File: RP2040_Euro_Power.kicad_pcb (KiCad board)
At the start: 2 copper layers, 110 x 110 mm, 150 parts, among them J1 Conn_01x40, J2 Conn_01x40, J3 Power, J4 USB C/USB 2.0, J5 Conn_01x03_Pin, SW1 SW_BOOT, SW2 SW_RESET, U1 78L05_SOT89, U2 W25Q128JVS, U3 TL431D, U4 AMS1117-3.3, U5 RP2040, U6 MCP6002, Y1 Crystal_12MHz_4Pin

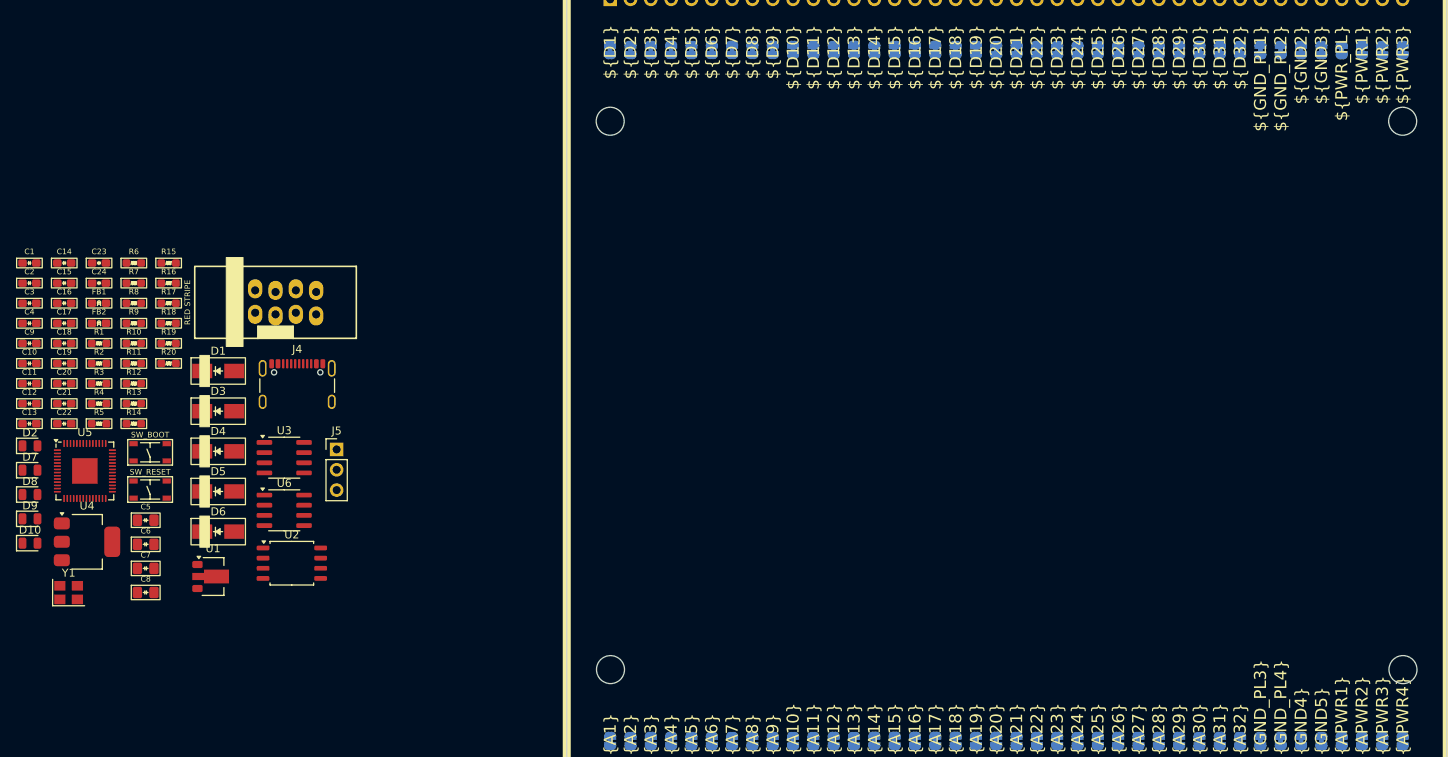
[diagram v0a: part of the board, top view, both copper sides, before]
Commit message: half of the parts placed on board
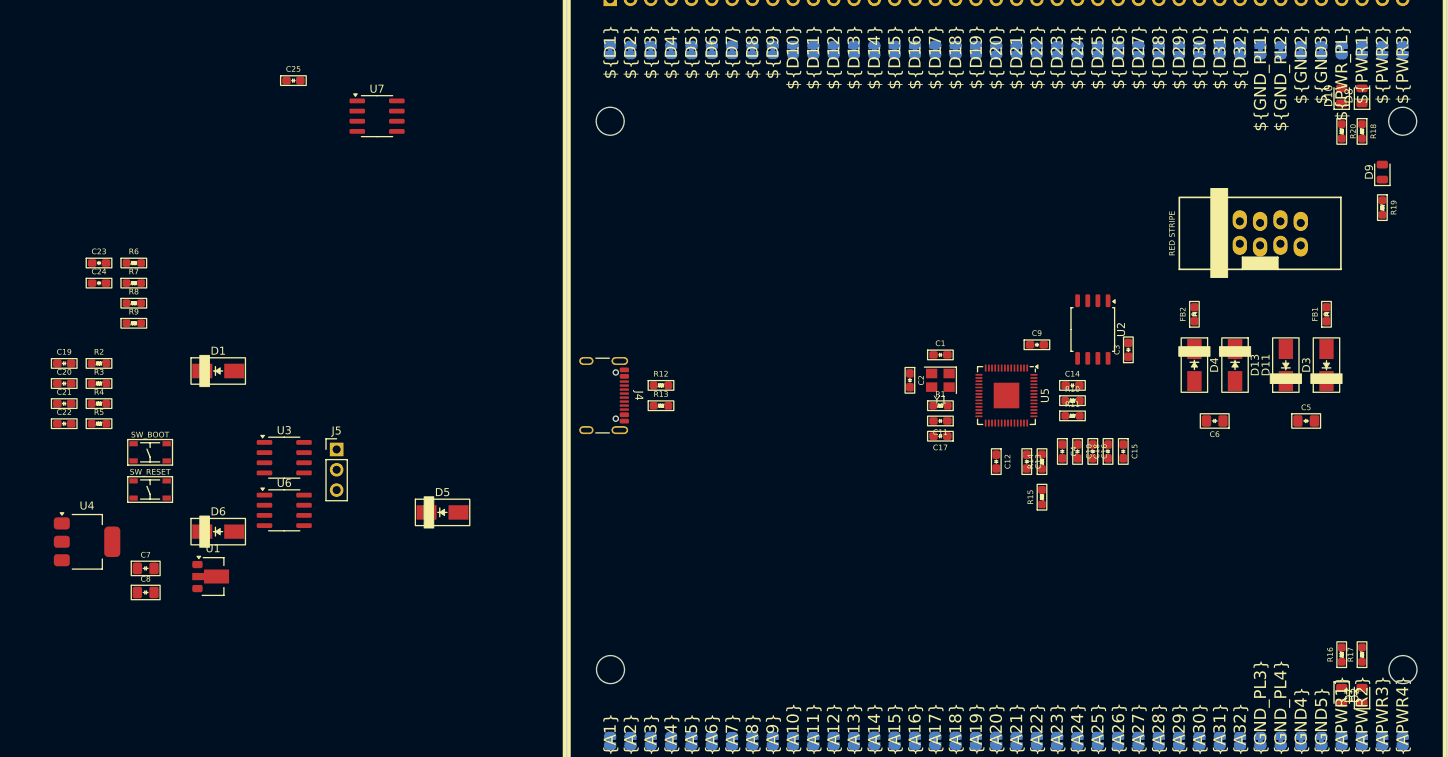
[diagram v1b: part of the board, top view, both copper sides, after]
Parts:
- added C25: 100n, winterbloom:C_0603_HandSolder, F.Cu at (39.8, 53.8)
- added D11: D_Schottky, winterbloom:D_SMA, F.Cu at (163.9, 89.4)
- added D13: D_Schottky, winterbloom:D_SMA, F.Cu at (157.5, 89.4)
- added U7: TL072, Package_SO:SOIC-8_3.9x4.9mm_P1.27mm, F.Cu at (50.3, 58.2)
- JP127, JP128, JP129, JP130: value ~ -> SolderJumper_2_Open; footprint Jumper:SolderJumper-2_P1.3mm_Bridged_RoundedPad1.0x1.5mm -> Jumper:SolderJumper-2_P1.3mm_Open_RoundedPad1.0x1.5mm
- R8: value 33k -> 47k
- moved D9 174.5 mm to (175.9, 65.2), turned to 90 degrees
- moved D8 173.8 mm to (173.4, 55.7), turned to 90 degrees
- moved D10 173.2 mm to (170.9, 55.7), turned to 90 degrees
- moved D7 168.9 mm to (173.4, 130.6), turned to 90 degrees
- moved D2 166.9 mm to (170.9, 130.6), turned to -90 degrees
- moved R17 155.5 mm to (173.4, 125.6), turned to 90 degrees
- moved R16 153.8 mm to (170.9, 125.6), turned to 90 degrees
- moved FB1 153.4 mm to (169.0, 83.0), turned to 90 degrees
- moved R19 152.7 mm to (175.9, 69.7), turned to -90 degrees
- moved R18 151.1 mm to (173.4, 60.2), turned to -90 degrees
- moved R20 149.5 mm to (170.9, 60.2), turned to -90 degrees
- moved C5 145.6 mm to (166.4, 96.3)
- moved D3 138.6 mm to (169.0, 89.4), turned to 90 degrees
- moved C3 137.5 mm to (144.2, 87.5), turned to 90 degrees
- moved FB2 136.9 mm to (152.5, 83.0), turned to 90 degrees
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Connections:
- C1 pad 1: GND -> GND_PLANE
- C10 pad 2: GND -> GND_PLANE
- C11 pad 2: GND -> GND_PLANE
- C12 pad 2: GND -> GND_PLANE
- C13 pad 2: GND -> GND_PLANE
- C14 pad 2: GND -> GND_PLANE
- C15 pad 2: GND -> GND_PLANE
- C16 pad 2: GND -> GND_PLANE
- C17 pad 2: GND -> GND_PLANE
- C18 pad 1: GND -> GND_PLANE
- C19 pad 1: PWR1 -> APWR1
- C19 pad 2: GND -> GND_PLANE
- C2 pad 1: GND -> GND_PLANE
- C20 pad 2: GND -> GND_PLANE
- C21 pad 2: GND -> GND_PLANE
- C22 pad 1: Net-(U6A--) -> Net-(U7A--)
- C22 pad 2: 3.3VREF -> 3VREF
- C23 pad 2: GND -> GND_PLANE
- C24 pad 2: GND -> GND_PLANE
- C3 pad 2: GND -> GND_PLANE
- C4 pad 2: GND -> GND_PLANE
- C5 pad 2: GND -> GND_PLANE
- C6 pad 2: GND -> GND_PLANE
- C7 pad 2: GND -> GND_PLANE
- C8 pad 2: GND -> GND_PLANE
- C9 pad 2: GND -> GND_PLANE
- D10 pad 1: GND -> Net-(D10-K)
- D10 pad 2: Net-(D10-A) -> IOVDD
- D2 pad 1: GND -> Net-(D2-K)
- D2 pad 2: Net-(D2-A) -> APWR1
- D7 pad 1: Net-(D7-K) -> APWR2
- D7 pad 2: GND -> Net-(D7-A)
- D8 pad 1: GND -> Net-(D8-K)
- D8 pad 2: Net-(D8-A) -> PWR1
- D9 pad 1: GND -> Net-(D9-K)
- D9 pad 2: Net-(D9-A) -> PWR2
- J3 pad 3: GND -> GND_PLANE
- J3 pad 4: GND -> GND_PLANE
- J3 pad 5: GND -> GND_PLANE
- J3 pad 6: GND -> GND_PLANE
- J3 pad 7: GND -> GND_PLANE
- J3 pad 8: GND -> GND_PLANE
- J4 pad A1: GND -> GND_PLANE
- J4 pad A12: GND -> GND_PLANE
- J4 pad B1: GND -> GND_PLANE
- J4 pad B12: GND -> GND_PLANE
- J4 pad S1: GND -> GND_PLANE
- J5 pad 1: SWCLK -> D27
- J5 pad 2: GND -> GND_PLANE
- J5 pad 3: SWD -> D28
- JP127 pad 1: Net-(J1-Pin_27) -> D27
- JP127 pad 2: D27 -> Net-(J1-Pin_27)
- JP128 pad 1: Net-(J1-Pin_28) -> D28
- JP128 pad 2: D28 -> Net-(J1-Pin_28)
- JP129 pad 1: Net-(J1-Pin_29) -> D29
- JP129 pad 2: D29 -> Net-(J1-Pin_29)
- JP130 pad 1: Net-(J1-Pin_30) -> BOOT
- JP130 pad 2: D30 -> Net-(J1-Pin_30)
- JP140 pad 2: 3.3VREF -> 3VREF
- R12 pad 2: GND -> GND_PLANE
- R13 pad 2: GND -> GND_PLANE
- R14 pad 1: 3.3VREF -> 3VREF
- R15 pad 2: 3.3VREF -> 3VREF
- R16 pad 1: APWR1 -> Net-(D2-K)
- R16 pad 2: Net-(D2-A) -> GND_PLANE
- R17 pad 1: APWR2 -> Net-(D7-A)
- R17 pad 2: Net-(D7-K) -> GND_PLANE
- R18 pad 1: PWR1 -> Net-(D8-K)
- R18 pad 2: Net-(D8-A) -> GND_PLANE
- R19 pad 1: PWR2 -> Net-(D9-K)
- R19 pad 2: Net-(D9-A) -> GND_PLANE
- R2 pad 1: Net-(SW1-A) -> BOOT
- R20 pad 1: IOVDD -> Net-(D10-K)
- R20 pad 2: Net-(D10-A) -> GND_PLANE
- R3 pad 2: Net-(SW1-A) -> BOOT
- R5 pad 1: Net-(SW1-A) -> BOOT
- R6 pad 1: RUN -> D29
- R7 pad 1: Net-(U6A--) -> Net-(U7A--)
- R7 pad 2: 3.3VREF -> 3VREF
- R8 pad 1: GND -> GND_PLANE
- R8 pad 2: Net-(U6A--) -> Net-(U7A--)
- SW1 pad 1: Net-(SW1-A) -> BOOT
- SW1 pad 2: GND -> GND_PLANE
- SW2 pad 1: RUN -> D29
- SW2 pad 2: GND -> GND_PLANE
- U1 pad 2: GND -> GND_PLANE
- U2 pad 4: GND -> GND_PLANE
- U3 pad 2: GND -> GND_PLANE
- U3 pad 3: GND -> GND_PLANE
- U3 pad 6: GND -> GND_PLANE
- U3 pad 7: GND -> GND_PLANE
- U4 pad 1: GND -> GND_PLANE
- U5 pad 19: GND -> GND_PLANE
- U5 pad 24: SWCLK -> D27
- U5 pad 25: SWD -> D28
- U5 pad 26: RUN -> D29
- U5 pad 57: GND -> GND_PLANE
- Y1 pad 2: GND -> GND_PLANE
- Y1 pad 4: GND -> GND_PLANE

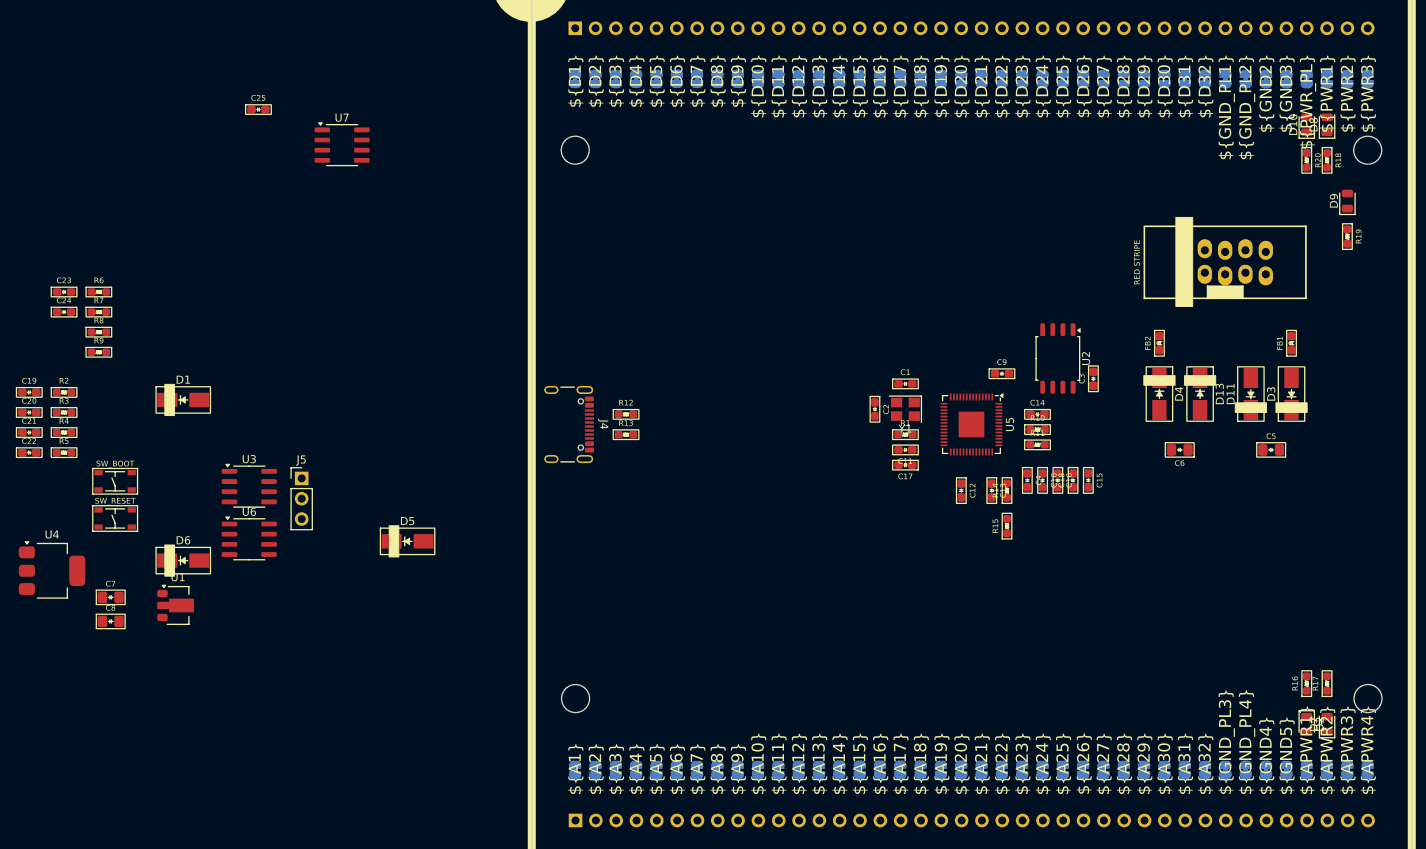
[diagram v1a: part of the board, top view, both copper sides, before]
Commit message: all parts placed on board
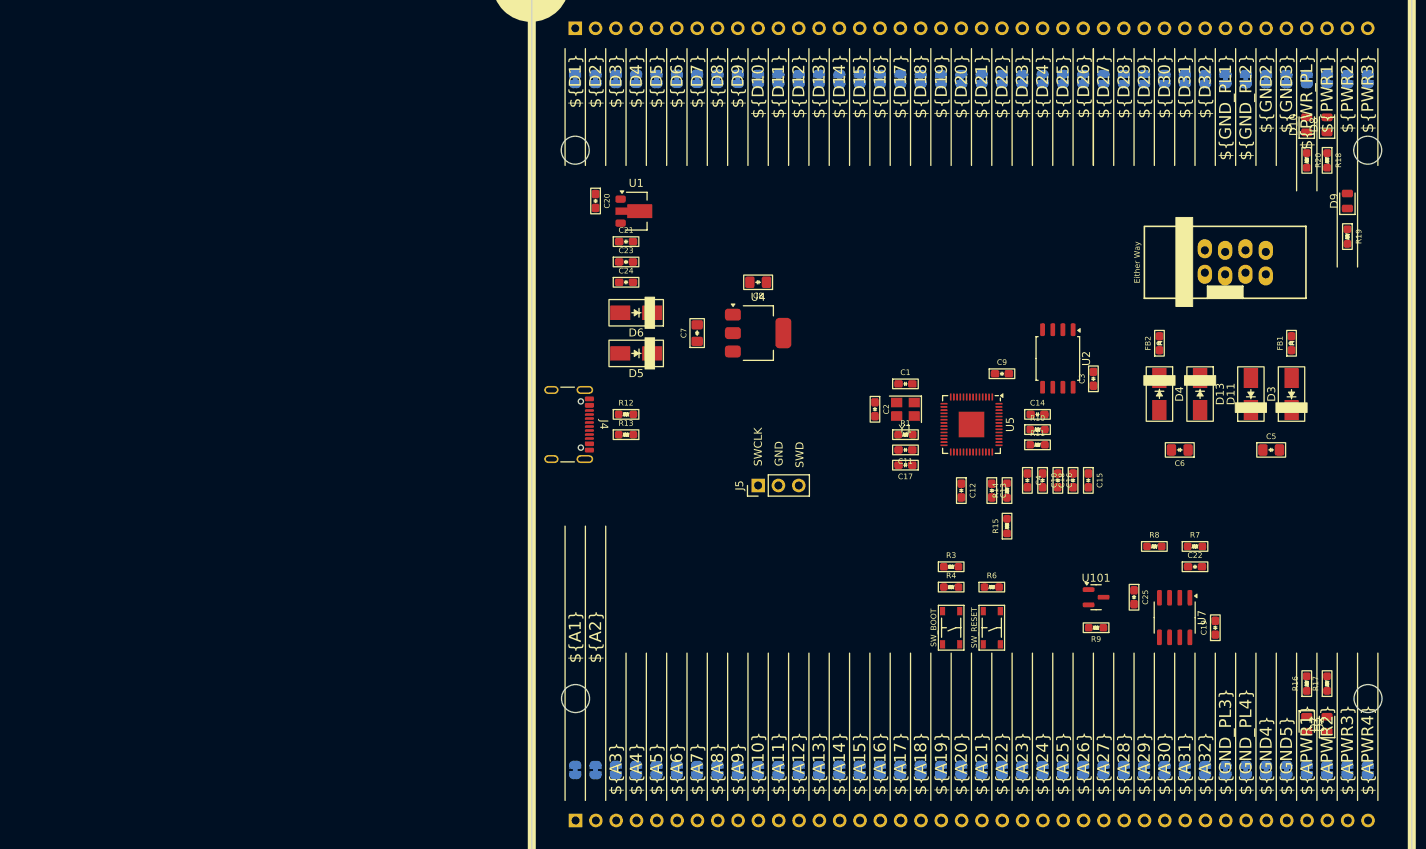
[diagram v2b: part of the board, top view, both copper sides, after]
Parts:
- removed D1: D_Schottky, winterbloom:D_SMA
- removed R2, R5: 10k, winterbloom:R_0603_HandSolder
- removed U3: TL431D, Package_SO:SOIC-8_3.9x4.9mm_P1.27mm
- removed U6: MCP6002, Package_SO:SOIC-8_3.9x4.9mm_P1.27mm
- added U101: TL431A, Package_TO_SOT_SMD:SOT-23, F.Cu at (144.5, 114.8)
- moved C19 151.1 mm to (159.4, 118.6), turned to 90 degrees
- moved C22 146.4 mm to (156.9, 111.0)
- moved R7 140.1 mm to (156.9, 108.4)
- moved R8 134.6 mm to (151.8, 108.4)
- moved R9 129.3 mm to (144.5, 118.6), turned to 180 degrees
- moved C25 125.3 mm to (149.3, 114.8), turned to -90 degrees
- moved U7 119.7 mm to (154.4, 117.3), turned to -90 degrees
- moved R6 117.6 mm to (131.5, 113.5)
- moved R4 112.6 mm to (126.4, 113.5)
- moved R3 112.5 mm to (126.4, 111.0)
- moved SW2 110.4 mm to (131.5, 118.6), turned to 90 degrees
- moved SW1 106.1 mm to (126.4, 118.6), turned to 90 degrees
- moved U4 93.1 mm to (102.3, 81.7)
- moved C8 91.4 mm to (102.3, 75.4), turned to 180 degrees
- moved C7 80.4 mm to (94.7, 81.7), turned to 90 degrees
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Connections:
- R3 pad 1: Net-(D1-K) -> QSPI_CS

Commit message: Board mostly layed out, ready to start routing
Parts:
- JP127, JP128, JP129, JP130: footprint Jumper:SolderJumper-2_P1.3mm_Open_RoundedPad1.0x1.5mm -> Jumper:SolderJumper-2_P1.3mm_Open_Pad1.0x1.5mm
- moved U1 49.0 mm to (90.2, 115.4), turned to -90 degrees
- moved C20 46.4 mm to (92.8, 110.4), turned to 180 degrees
- moved J5 41.3 mm to (142.9, 108.4), turned to -90 degrees
- moved C21 40.1 mm to (87.7, 110.4)
- moved C8 36.9 mm to (99.7, 112.2), turned to 90 degrees
- moved C23 35.0 mm to (87.7, 107.8)
- moved U4 30.6 mm to (105.5, 112.2), turned to -90 degrees
- moved C24 30.0 mm to (87.7, 105.3)
- moved D6 26.1 mm to (106.1, 97.0), turned to 90 degrees
- moved C7 25.3 mm to (105.5, 104.6), turned to 0 degrees
- moved D5 18.9 mm to (101.0, 97.0), turned to 90 degrees
- moved R7 10.0 mm to (166.4, 105.2)
- moved R8 10.0 mm to (161.3, 105.2)
- moved U7 10.0 mm to (163.9, 114.1)
- moved C22 10.0 mm to (166.4, 107.8)
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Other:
- board text added: "+3.3v"
- board text added: "+5v"
- board text added: "3vref"
- board text added: "Eurorack Power"
- board text added: "RP2040"
- board text added: "USB-C"
